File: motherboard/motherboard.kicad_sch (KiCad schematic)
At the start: 1 part, among them J20 CM3588 Hirose Connector

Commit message: audio done
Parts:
- added C80, C81: 10uF, Capacitor_SMD:C_0402_1005Metric, symbol Device:C_Small
- added U26: AMS1117-1.8, Package_TO_SOT_SMD:SOT-223-3_TabPin2, symbol Regulator_Linear:AMS1117-1.8
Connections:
- net GND: now also C80.2, C81.2, U26.1 (GND)
- new net +1V8: C81.1, U26.2 (VO)
- new net +5V: C80.1, U26.3 (VI)
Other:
- sheet System ports: added GPIO4_C2/HALL_OUT; removed none
- note added: "@TODO: need way to accept 5v and 3.3v input from pwr board"

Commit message: motherboard schematic done
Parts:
- added C82: 100nF, Capacitor_SMD:C_0402_1005Metric, symbol Device:C_Small
- added C83, C87, C88: 10uF, Capacitor_SMD:C_0402_1005Metric, symbol Device:C_Small
- added C84: 1uF, Capacitor_SMD:C_0402_1005Metric, symbol Device:C_Small
- added C85: 1nF, Capacitor_SMD:C_0402_1005Metric, symbol Device:C_Small
- added C86: 10pF, Capacitor_SMD:C_0402_1005Metric, symbol Device:C_Small
- added C89: 8.2nF, Capacitor_SMD:C_0402_1005Metric, symbol Device:C_Small
- added D8: SS54, Diode_SMD:D_SMA, symbol Device:D_Schottky
- added L2: 3.3uH, Inductor_SMD:L_Vishay_IHLP-1616, symbol Device:L_Small
- added R112: 24k, Resistor_SMD:R_0402_1005Metric, symbol Device:R_Small
- added R113: 2k, Resistor_SMD:R_0402_1005Metric, symbol Device:R_Small
- added R114: 10k, Resistor_SMD:R_0402_1005Metric, symbol Device:R_Small
- added R115: 3.3k, Resistor_SMD:R_0402_1005Metric, symbol Device:R_Small
- added U27: TPS54331DR, TPS54331DR:SOIC127P599X175-8N, symbol TPS54331DR:TPS54331DR
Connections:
- net +5V: now also C87.1, C88.1, U27.2 (VIN)
- net GND: now also C83.2, C84.2, C85.2, C86.2, C87.2, C88.2, C89.2, D8.2 (A), R115.2, U27.7 (GND)
- new net: C89.1, U27.4 (SS)
- new net: C86.1, R112.1, U27.6 (COMP)
- new net: R112.2, R113.1
- new net: C85.1, R113.2
- new net: C82.1, U27.1 (BOOT)
- new net: C82.2, D8.1 (K), L2.2, U27.8 (PH)
- new net: R114.2, R115.1, U27.5 (VSENSE)
- new net +3.3V: C83.1, C84.1, L2.1, R114.1
- new net EN: U27.3 (EN)
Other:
- sheet Audio ports: added GPIO1_C4/HP_DET_L, HPL, HPR, L_AMP_SCL, L_AMP_SDA, MIC_IN, R_AMP_SCL, R_AMP_SDA, SPK_EN; removed none
- sheet System ports: added FSPI_CLK, FSPI_CSN0, FSPI_D0, FSPI_D1, FSPI_D2, FSPI_D3; removed none
- sheet eDP ports: added AUX_N, AUX_P, BIST_EN, DP_0N, DP_0P, DP_1N, DP_1P, DP_2N, DP_2P, DP_3N, DP_3P; removed none
- note added: "<- 12v? (says 6-21v)"
- note added: "<- self defined"
- note added: "SDIO_M0"
- note added: "pinout from radxa FSPI_M2"

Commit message: work preparing for routing
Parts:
- added C92, C93: 10uF, Capacitor_SMD:C_0402_1005Metric, symbol Device:C_Small
- added J21: 5V IN, Connector_JST:JST_GH_SM10B-GHS-TB_1x10-1MP_P1.25mm_Horizontal, symbol Connector_Generic_MountingPin:Conn_01x10_MountingPin
- added J22: BATTERY IN, Connector_JST:JST_GH_SM10B-GHS-TB_1x10-1MP_P1.25mm_Horizontal, symbol Connector_Generic_MountingPin:Conn_01x10_MountingPin
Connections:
- net +5V: now also C92.1, C93.1, J21.1 (Pin_1), J21.2 (Pin_2), J21.3 (Pin_3), J21.4 (Pin_4), J21.5 (Pin_5)
- net GND: now also C92.2, C93.2, J21.10 (Pin_10), J21.6 (Pin_6), J21.7 (Pin_7), J21.8 (Pin_8), J21.9 (Pin_9), J21.MP (MountPin), J22.10 (Pin_10), J22.6 (Pin_6), J22.7 (Pin_7), J22.8 (Pin_8), J22.9 (Pin_9), J22.MP (MountPin)
- net VDD: now also J22.1 (Pin_1), J22.2 (Pin_2), J22.3 (Pin_3), J22.4 (Pin_4), J22.5 (Pin_5)
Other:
- note added: "@TODO: need way to accept 5v"
- note removed: "@TODO: need way to accept 5v and 3.3v input from pwr board"
- moved on the sheet: C80, C81, C82, C83, C84, C85, C86, C87, C88, C89, D8, J20A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

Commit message: minor motherboard work
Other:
- note removed: "@TODO: need way to accept 5v"
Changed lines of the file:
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@@
-		)
-	)
-	(text "@TODO: need way to accept 5v"
-		(exclude_from_sim no)
-		(at 97.536 196.088 0)
-		(effects
-			(font
-				(face "JetBrains Mono NL")
-				(size 5 5)
-				(thickness 1)
-				(bold yes)
-				(italic yes)
-			)
 		)
 	)

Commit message: layout nearing completion
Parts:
- C80, C81, C83, C87, C88, C92, C93: footprint Capacitor_SMD:C_0402_1005Metric -> Capacitor_SMD:C_0603_1608Metric
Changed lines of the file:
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@@
 	(text "2k2 pull up device side"
 		(exclude_from_sim no)
-		(at 119.634 297.434 0)
+		(at 119.888 298.196 0)
 		(effects
 			(font
@@
 			)
 		)
-		(property "Footprint" "Capacitor_SMD:C_0402_1005Metric"
+		(property "Footprint" "Capacitor_SMD:C_0603_1608Metric"
 			(at 186.69 190.5 0)
 			(effects
@@
 			)
 		)
-		(property "Footprint" "Capacitor_SMD:C_0402_1005Metric"
+		(property "Footprint" "Capacitor_SMD:C_0603_1608Metric"
 			(at 373.38 200.66 0)
 			(effects
@@
 			)
 		)
-		(property "Footprint" "Capacitor_SMD:C_0402_1005Metric"
+		(property "Footprint" "Capacitor_SMD:C_0603_1608Metric"
 			(at 313.69 179.07 0)
 			(effects
@@
 			)
 		)
-		(property "Footprint" "Capacitor_SMD:C_0402_1005Metric"
+		(property "Footprint" "Capacitor_SMD:C_0603_1608Metric"
 			(at 420.37 212.09 0)
 			(effects
@@
 			)
 		)
-		(property "Footprint" "Capacitor_SMD:C_0402_1005Metric"
+		(property "Footprint" "Capacitor_SMD:C_0603_1608Metric"
 			(at 416.56 212.09 0)
 			(effects
@@
 			)
 		)
-		(property "Footprint" "Capacitor_SMD:C_0402_1005Metric"
+		(property "Footprint" "Capacitor_SMD:C_0603_1608Metric"
 			(at 334.01 179.07 0)
 			(effects
@@
 			)
 		)
-		(property "Footprint" "Capacitor_SMD:C_0402_1005Metric"
+		(property "Footprint" "Capacitor_SMD:C_0603_1608Metric"
 			(at 191.77 190.5 0)
 			(effects

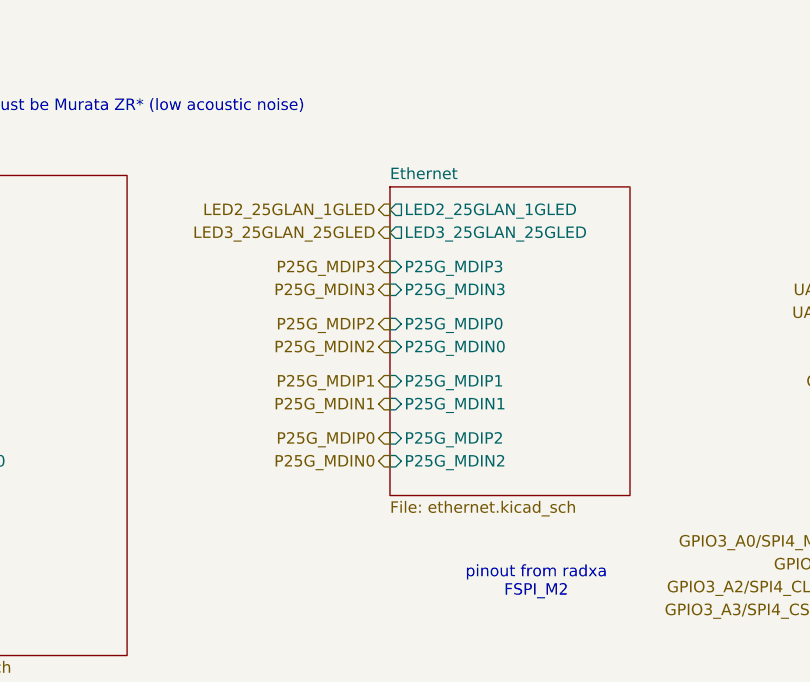
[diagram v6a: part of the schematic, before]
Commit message: removed 2.5G ethernet
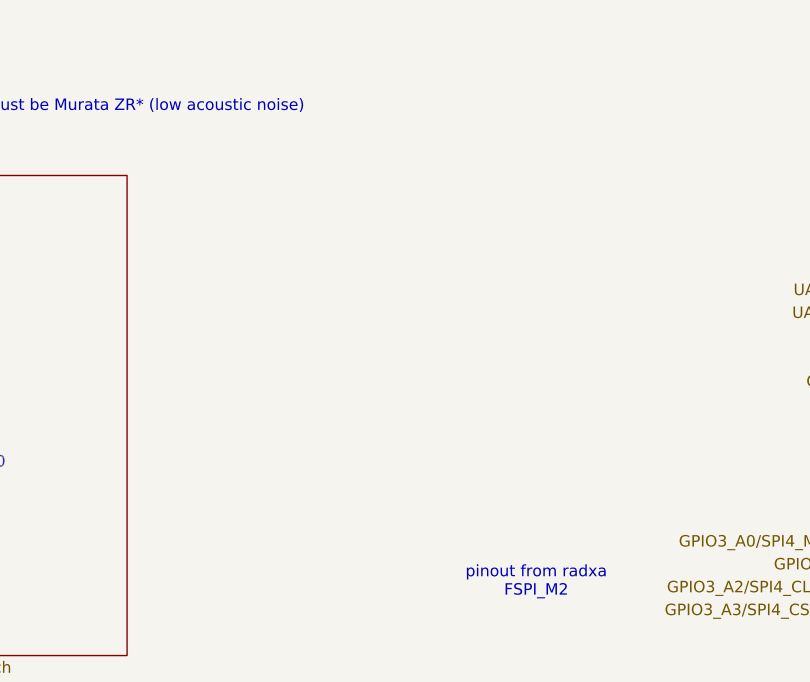
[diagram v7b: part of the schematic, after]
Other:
- removed sheet Ethernet
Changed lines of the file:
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@@
 		)
 	)
-	(hierarchical_label "P25G_MDIP1"
-		(shape output)
-		(at 133.35 245.11 180)
-		(fields_autoplaced yes)
-		(effects
-			(font
-				(size 1.27 1.27)
-			)
-			(justify right)
-		)
-	)
 	(hierarchical_label "PCIE30_PORT0_TX1N"
 		(shape output)
@@
 		)
 	)
-	(hierarchical_label "P25G_MDIN2"
-		(shape output)
-		(at 133.35 241.3 180)
-		(fields_autoplaced yes)
-		(effects
-			(font
-				(size 1.27 1.27)
-			)
-			(justify right)
-		)
-	)
 	(hierarchical_label "GPIO2_C0"
 		(shape output)
@@
 		)
 	)
-	(hierarchical_label "P25G_MDIP2"
-		(shape output)
-		(at 133.35 238.76 180)
-		(fields_autoplaced yes)
-		(effects
-			(font
-				(size 1.27 1.27)
-			)
-			(justify right)
-		)
-	)
 	(hierarchical_label "PCIE20_2_RXN"
 		(shape input)
@@
 		)
 	)
-	(hierarchical_label "LED3_25GLAN_25GLED"
-		(shape output)
-		(at 133.35 228.6 180)
-		(fields_autoplaced yes)
-		(effects
-			(font
-				(size 1.27 1.27)
-			)
-			(justify right)
-		)
-	)
 	(hierarchical_label "GPIO3_C0{slash}TP_INT_L"
 		(shape output)
@@
 		)
 	)
-	(hierarchical_label "P25G_MDIN0"
-		(shape output)
-		(at 133.35 254 180)
-		(fields_autoplaced yes)
-		(effects
-			(font
-				(size 1.27 1.27)
-			)
-			(justify right)
-		)
-	)
 	(hierarchical_label "I2C6_SDA_M0"
 		(shape bidirectional)
@@
 		)
 	)
-	(hierarchical_label "P25G_MDIN1"
-		(shape output)
-		(at 133.35 247.65 180)
-		(fields_autoplaced yes)
-		(effects
-			(font
-				(size 1.27 1.27)
-			)
-			(justify right)
-		)
-	)
 	(hierarchical_label "MIPI_DPHY0_TX_D1P"
 		(shape output)
@@
 		)
 	)
-	(hierarchical_label "P25G_MDIN3"
-		(shape output)
-		(at 133.35 234.95 180)
-		(fields_autoplaced yes)
-		(effects
-			(font
-				(size 1.27 1.27)
-			)
-			(justify right)
-		)
-	)
 	(hierarchical_label "MIPI_DPHY1_RX_D2N"
 		(shape output)
@@
 		)
 	)
-	(hierarchical_label "P25G_MDIP0"
-		(shape output)
-		(at 133.35 251.46 180)
-		(fields_autoplaced yes)
-		(effects
-			(font
-				(size 1.27 1.27)
-			)
-			(justify right)
-		)
-	)
 	(hierarchical_label "HDMITX1_SDA_M1"
 		(shape bidirectional)
@@
 		)
 	)
-	(hierarchical_label "LED2_25GLAN_1GLED"
-		(shape output)
-		(at 133.35 226.06 180)
-		(fields_autoplaced yes)
-		(effects
-			(font
-				(size 1.27 1.27)
-			)
-			(justify right)
-		)
-	)
 	(hierarchical_label "PCIE30_PORT0_TX0N"
 		(shape output)
@@
 		)
 	)
-	(hierarchical_label "P25G_MDIP3"
-		(shape output)
-		(at 133.35 232.41 180)
-		(fields_autoplaced yes)
-		(effects
-			(font
-				(size 1.27 1.27)
-			)
-			(justify right)
-		)
-	)
 	(hierarchical_label "MIPI_CSI1_RX_D1N"
 		(shape output)
@@
 				)
 			)
-		)
-	)
-	(sheet
-		(at 133.35 223.52)
-		(size 26.67 34.29)
-		(fields_autoplaced yes)
-		(stroke
-			(width 0.1524)
-			(type solid)
-		)
-		(fill
-			(color 0 0 0 0.0000)
-		)
-		(property "Sheetname" "Ethernet"
-			(at 133.35 222.8084 0)
-			(effects
-				(font
-					(size 1.27 1.27)
-				)
-				(justify left bottom)
-			)
-		)
-		(property "Sheetfile" "ethernet.kicad_sch"
-			(at 133.35 258.3946 0)
-			(effects
-				(font
-					(size 1.27 1.27)
-				)
-				(justify left top)
-			)
-		)
-		(pin "LED2_25GLAN_1GLED" output
-			(at 133.35 226.06 180)
-			(effects
-				(font
-					(size 1.27 1.27)
-				)
-				(justify left)
-			)
-		)
-		(pin "LED3_25GLAN_25GLED" output
-			(at 133.35 228.6 180)
-			(effects
-				(font
-					(size 1.27 1.27)
-				)
-				(justify left)
-			)
-		)
-		(pin "P25G_MDIN2" input
-			(at 133.35 254 180)
-			(effects
-				(font
-					(size 1.27 1.27)
-				)
-				(justify left)
-			)
-		)
-		(pin "P25G_MDIP3" input
-			(at 133.35 232.41 180)
-			(effects
-				(font
-					(size 1.27 1.27)
-				)
-				(justify left)
-			)
-		)
-		(pin "P25G_MDIN3" input
-			(at 133.35 234.95 180)
-			(effects
-				(font
-					(size 1.27 1.27)
-				)
-				(justify left)
-			)
-		)
-		(pin "P25G_MDIP2" input
-			(at 133.35 251.46 180)
-			(effects
-				(font
-					(size 1.27 1.27)
-				)
-				(justify left)
-			)
-		)
-		(pin "P25G_MDIP0" input
-			(at 133.35 238.76 180)
-			(effects
-				(font
-					(size 1.27 1.27)
-				)
-				(justify left)
-			)
-		)
-		(pin "P25G_MDIP1" input
-			(at 133.35 245.11 180)
-			(effects
-				(font
-					(size 1.27 1.27)
-				)
-				(justify left)
-			)
-		)
-		(pin "P25G_MDIN0" input
-			(at 133.35 241.3 180)
-			(effects
-				(font
-					(size 1.27 1.27)
-				)
-				(justify left)
-			)
-		)
-		(pin "P25G_MDIN1" input
-			(at 133.35 247.65 180)
-			(effects
-				(font
-					(size 1.27 1.27)
-				)
-				(justify left)
-			)
-		)
-		(instances
-			(project "motherboard"
-				(path "/025fe4d1-0305-4b34-be04-f8d9818125a4"
-					(page "8")
-				)
-			)

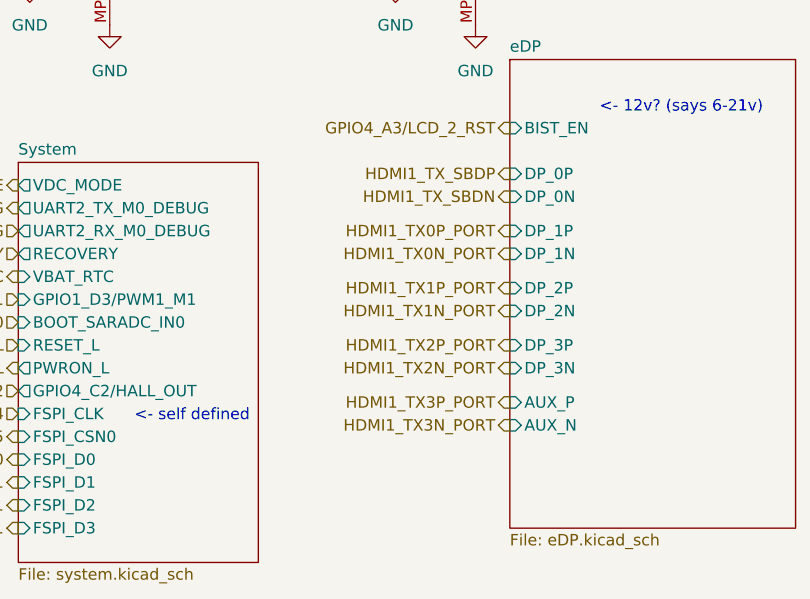
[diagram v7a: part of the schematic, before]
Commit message: created display evaluation board + layout modifications
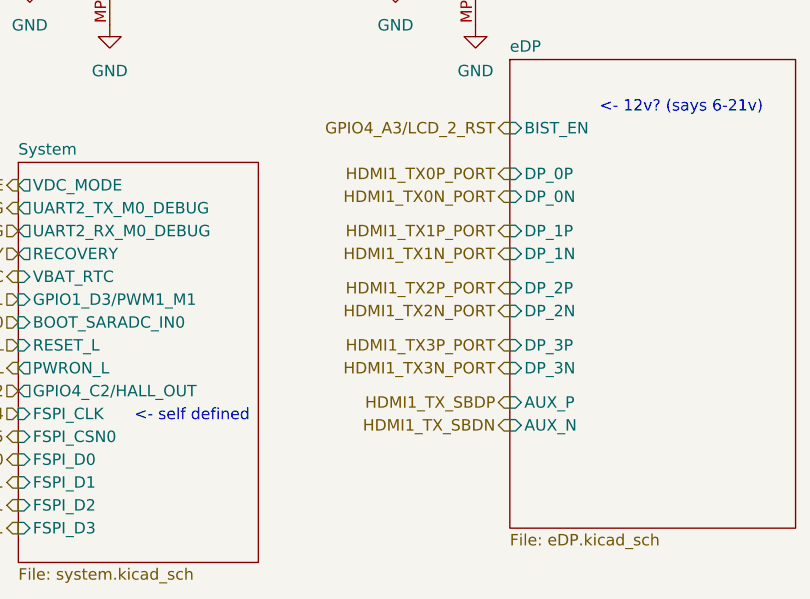
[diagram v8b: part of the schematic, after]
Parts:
- J21, J22: footprint Connector_JST:JST_GH_SM10B-GHS-TB_1x10-1MP_P1.25mm_Horizontal -> Connector_Molex:Molex_PicoBlade_53398-1071_1x10-1MP_P1.25mm_Vertical
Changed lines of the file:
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@@
 		)
 	)
-	(hierarchical_label "HDMI1_TX2P_PORT"
-		(shape output)
-		(at 254 250.19 180)
-		(fields_autoplaced yes)
-		(effects
-			(font
-				(size 1.27 1.27)
-			)
-			(justify right)
-		)
-	)
 	(hierarchical_label "GPIO4_B3"
 		(shape output)
@@
 		)
 	)
+	(hierarchical_label "HDMI1_TX3P_PORT"
+		(shape output)
+		(at 254 250.19 180)
+		(fields_autoplaced yes)
+		(effects
+			(font
+				(size 1.27 1.27)
+			)
+			(justify right)
+		)
+	)
 	(hierarchical_label "HDMI1_TX1P_PORT"
 		(shape output)
@@
 		)
 	)
-	(hierarchical_label "HDMI1_TX1P_PORT"
-		(shape output)
-		(at 254 243.84 180)
-		(fields_autoplaced yes)
-		(effects
-			(font
-				(size 1.27 1.27)
-			)
-			(justify right)
-		)
-	)
 	(hierarchical_label "VDC_MODE"
 		(shape output)
@@
 		)
 	)
-	(hierarchical_label "HDMI1_TX2N_PORT"
-		(shape output)
-		(at 254 252.73 180)
-		(fields_autoplaced yes)
-		(effects
-			(font
-				(size 1.27 1.27)
-			)
-			(justify right)
-		)
-	)
 	(hierarchical_label "GPIO2_B7"
 		(shape output)
@@
 		)
 	)
-	(hierarchical_label "HDMI1_TX3N_PORT"
-		(shape output)
-		(at 254 259.08 180)
-		(fields_autoplaced yes)
-		(effects
-			(font
-				(size 1.27 1.27)
-			)
-			(justify right)
-		)
-	)
 	(hierarchical_label "TYPEC1_SSTX1N"
 		(shape output)
@@
 		)
 	)
-	(hierarchical_label "HDMI1_TX0N_PORT"
-		(shape output)
-		(at 254 240.03 180)
-		(fields_autoplaced yes)
-		(effects
-			(font
-				(size 1.27 1.27)
-			)
-			(justify right)
-		)
-	)
 	(hierarchical_label "PCIE20_1_TXN"
 		(shape output)
@@
 		)
 	)
-	(hierarchical_label "HDMI1_TX3P_PORT"
-		(shape output)
-		(at 254 256.54 180)
-		(fields_autoplaced yes)
-		(effects
-			(font
-				(size 1.27 1.27)
-			)
-			(justify right)
-		)
-	)
 	(hierarchical_label "MIPI_DPHY1_TX_D3P"
 		(shape output)
@@
 		)
 	)
+	(hierarchical_label "HDMI1_TX0N_PORT"
+		(shape output)
+		(at 254 233.68 180)
+		(fields_autoplaced yes)
+		(effects
+			(font
+				(size 1.27 1.27)
+			)
+			(justify right)
+		)
+	)
 	(hierarchical_label "I2C6_SCL_M0"
 		(shape input)
@@
 		)
 	)
+	(hierarchical_label "HDMI1_TX1P_PORT"
+		(shape output)
+		(at 254 237.49 180)
+		(fields_autoplaced yes)
+		(effects
+			(font
+				(size 1.27 1.27)
+			)
+			(justify right)
+		)
+	)
 	(hierarchical_label "PWRON_L"
 		(shape output)
@@
 		)
 	)
+	(hierarchical_label "HDMI1_TX0P_PORT"
+		(shape output)
+		(at 254 231.14 180)
+		(fields_autoplaced yes)
+		(effects
+			(font
+				(size 1.27 1.27)
+			)
+			(justify right)
+		)
+	)
 	(hierarchical_label "GPIO1_D3{slash}PWM1_M1"
 		(shape input)
@@
 		)
 	)
-	(hierarchical_label "HDMI1_TX_SBDP"
+	(hierarchical_label "P25G_MDIN2"
 		(shape output)
-		(at 254 231.14 180)
+		(at 106.68 154.94 0)
 		(fields_autoplaced yes)
 		(effects
@@
 				(size 1.27 1.27)
 			)
-			(justify right)
+			(justify left)
 		)
 	)
-	(hierarchical_label "P25G_MDIN2"
-		(shape output)
-		(at 106.68 154.94 0)
+	(hierarchical_label "TYPEC1_SSRX1N"
+		(shape input)
+		(at 213.36 327.66 0)
 		(fields_autoplaced yes)
 		(effects
@@
 		)
 	)
-	(hierarchical_label "TYPEC1_SSRX1N"
-		(shape input)
-		(at 213.36 327.66 0)
+	(hierarchical_label "HDMI1_TX_SBDN"
+		(shape output)
+		(at 254 259.08 180)
 		(fields_autoplaced yes)
 		(effects
@@
 				(size 1.27 1.27)
 			)
-			(justify left)
+			(justify right)
 		)
 	)
@@
 		)
 	)
+	(hierarchical_label "HDMI1_TX2P_PORT"
+		(shape output)
+		(at 254 243.84 180)
+		(fields_autoplaced yes)
+		(effects
+			(font
+				(size 1.27 1.27)
+			)
+			(justify right)
+		)
+	)
 	(hierarchical_label "I2C6_SDA_M0"
 		(shape bidirectional)
@@
 		)
 	)
-	(hierarchical_label "HDMI1_TX_SBDN"
-		(shape output)
-		(at 254 233.68 180)
-		(fields_autoplaced yes)
-		(effects
-			(font
-				(size 1.27 1.27)
-			)
-			(justify right)
-		)
-	)
 	(hierarchical_label "HDMI0_TX2P_PORT"
 		(shape bidirectional)
@@
 		)
 	)
-	(hierarchical_label "LED3_25GLAN_25GLED"
+	(hierarchical_label "HDMI1_TX1N_PORT"
 		(shape output)
-		(at 106.68 129.54 0)
+		(at 254 240.03 180)
 		(fields_autoplaced yes)
 		(effects
@@
 				(size 1.27 1.27)
 			)
-			(justify left)
-		)
-	)
-	(hierarchical_label "MIPI_DPHY1_RX_CLKN"
-		(shape output)
-		(at 191.77 93.98 0)
-		(fields_autoplaced yes)
-		(effects
-			(font
-				(size 0.001 0.001)
-			)
-			(justify left)
+			(justify right)
 		)
 	)
-	(hierarchical_label "HDMI1_TX1N_PORT"
+	(hierarchical_label "LED3_25GLAN_25GLED"
 		(shape output)
-		(at 254 246.38 180)
+		(at 106.68 129.54 0)
 		(fields_autoplaced yes)
 		(effects
@@
 				(size 1.27 1.27)
 			)
-			(justify right)
+			(justify left)
 		)
 	)
-	(hierarchical_label "HDMI1_TX0P_PORT"
+	(hierarchical_label "MIPI_DPHY1_RX_CLKN"
 		(shape output)
-		(at 254 237.49 180)
+		(at 191.77 93.98 0)
 		(fields_autoplaced yes)
 		(effects
 			(font
-				(size 1.27 1.27)
+				(size 0.001 0.001)
 			)
-			(justify right)
+			(justify left)
 		)
 	)
@@
 		)
 	)
+	(hierarchical_label "HDMI1_TX2N_PORT"
+		(shape output)
+		(at 254 246.38 180)
+		(fields_autoplaced yes)
+		(effects
+			(font
+				(size 1.27 1.27)
+			)
+			(justify right)
+		)
+	)
 	(hierarchical_label "SDMMC0_D2"
 		(shape bidirectional)
@@
 		)
 	)
+	(hierarchical_label "HDMI1_TX3N_PORT"
+		(shape output)
+		(at 254 252.73 180)
+		(fields_autoplaced yes)
+		(effects
+			(font
+				(size 1.27 1.27)
+			)
+			(justify right)
+		)
+	)
 	(hierarchical_label "TYPEC0_SSTX2P"
 		(shape output)
@@
 		)
 	)
+	(hierarchical_label "HDMI1_TX_SBDP"
+		(shape output)
+		(at 254 256.54 180)
+		(fields_autoplaced yes)
+		(effects
+			(font
+				(size 1.27 1.27)
+			)
+			(justify right)
+		)
+	)
 	(hierarchical_label "UART2_TX_M0_DEBUG"
 		(shape output)
@@
 			)
 		)
-		(property "Footprint" "Connector_JST:JST_GH_SM10B-GHS-TB_1x10-1MP_P1.25mm_Horizontal"
+		(property "Footprint" "Connector_Molex:Molex_PicoBlade_53398-1071_1x10-1MP_P1.25mm_Vertical"
 			(at 209.55 196.85 0)
 			(effects
@@
 			)
 		)
-		(property "Footprint" "Connector_JST:JST_GH_SM10B-GHS-TB_1x10-1MP_P1.25mm_Horizontal"
+		(property "Footprint" "Connector_Molex:Molex_PicoBlade_53398-1071_1x10-1MP_P1.25mm_Vertical"
 			(at 250.19 196.85 0)
 			(effects
